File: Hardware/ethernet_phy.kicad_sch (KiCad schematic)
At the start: 17 parts, among them T1 WE-RJ45_7499010211A, U5 DP83822IRHBR

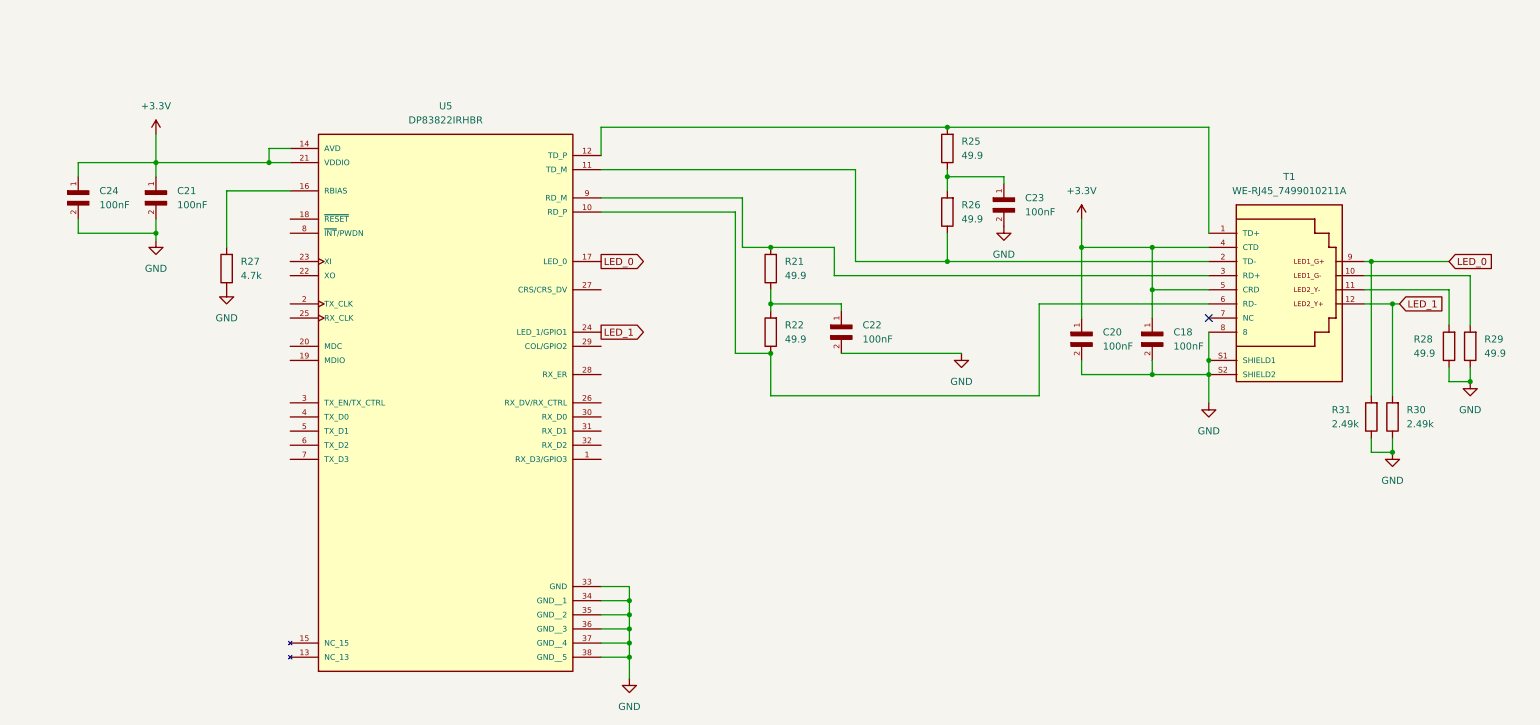
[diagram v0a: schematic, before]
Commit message: Finished Ethernet connection between MAC and PHY
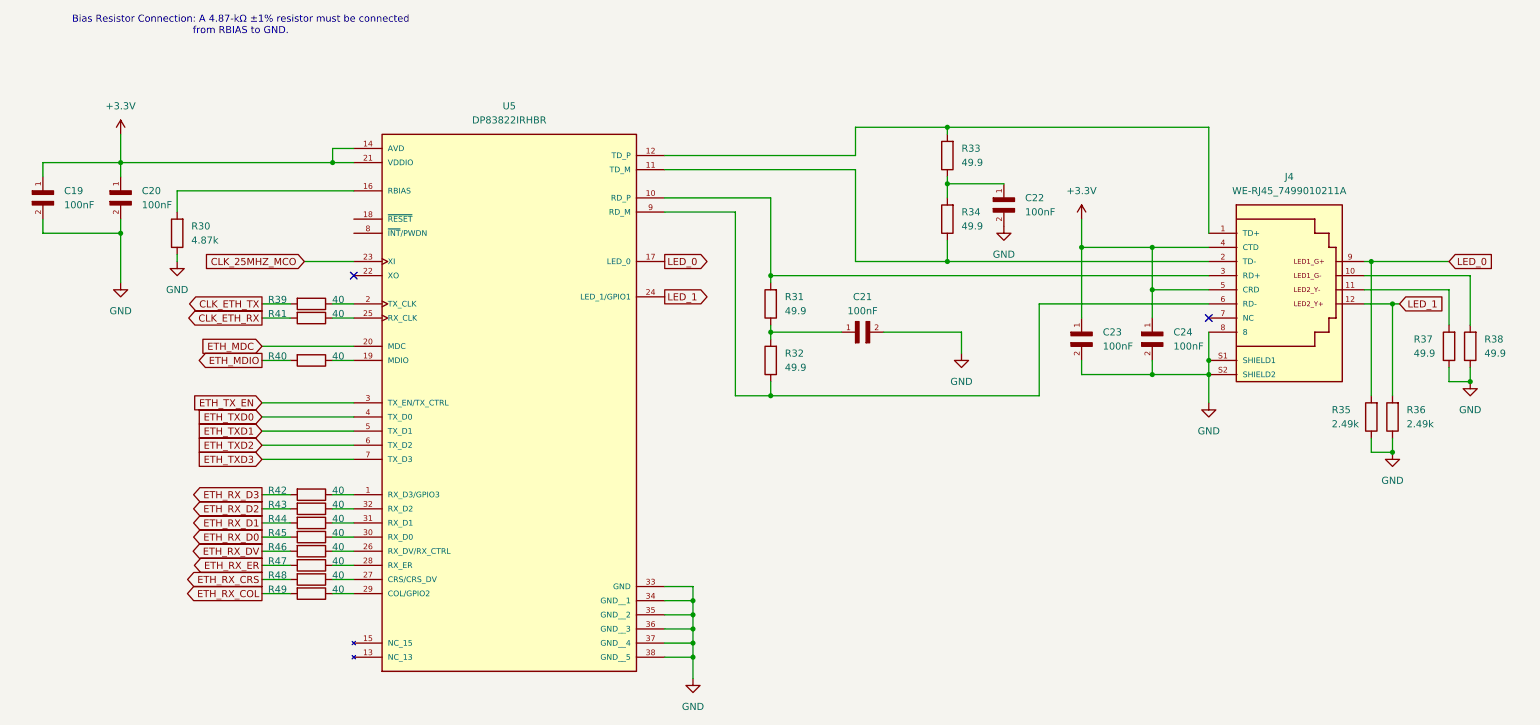
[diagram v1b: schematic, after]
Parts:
- added R39, R40, R41, R42, R43, R44, R45, R46, R47, R48, R49: 40, Resistor_SMD:R_0402_1005Metric, symbol Device:R
- R30: renamed from R27; value 4.7k -> 4.87k
- renumbered C24 to C19, C21 to C20, C22 to C21, C23 to C22, C20 to C23, C18 to C24, T1 to J4, R21 to R31, R22 to R32, R25 to R33, R26 to R34, R31 to R35, R30 to R36, R28 to R37, R29 to R38
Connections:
- net at U5.1 (RX_D3/GPIO3): now also R42.1
- net at J4.6 (RD-), R32.1: now also U5.9 (RD_M); no longer U5.10 (RD_P)
- net at U5.19 (MDIO): now also R40.1
- net at U5.2 (TX_CLK): now also R39.1
- net ETH_MDC: now reaches U5.20 (MDC)
- net CLK_25MHZ_MCO: now reaches U5.23 (XI)
- net at U5.25 (RX_CLK): now also R41.1
- net at U5.26 (RX_DV/RX_CTRL): now also R46.1
- net at U5.27 (CRS/CRS_DV): now also R48.1
- net at U5.28 (RX_ER): now also R47.1
- net at U5.29 (COL/GPIO2): now also R49.1
- net ETH_TX_EN: now reaches U5.3 (TX_EN/TX_CTRL)
- net at U5.30 (RX_D0): now also R45.1
- net at U5.31 (RX_D1): now also R44.1
- net at U5.32 (RX_D2): now also R43.1
- net ETH_TXD0: now reaches U5.4 (TX_D0)
- net ETH_TXD1: now reaches U5.5 (TX_D1)
- net ETH_TXD2: now reaches U5.6 (TX_D2)
- net ETH_TXD3: now reaches U5.7 (TX_D3)
- net at J4.3 (RD+), R31.2: now also U5.10 (RD_P); no longer U5.9 (RD_M)
- new net CLK_ETH_RX: R41.2
- new net CLK_ETH_TX: R39.2
- new net ETH_MDIO: R40.2
- new net ETH_RX_COL: R49.2
- new net ETH_RX_CRS: R48.2
- new net ETH_RX_D0: R45.2
- new net ETH_RX_D1: R44.2
- new net ETH_RX_D2: R43.2
- new net ETH_RX_D3: R42.2
- new net ETH_RX_DV: R46.2
- new net ETH_RX_ER: R47.2
- no-connect marks 1 -> 2
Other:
- note added: "Bias Resistor Connection: A 4.87-kΩ ±1% resistor must be connected from RBIAS to GND."
- moved on the sheet: C19, C20, C21, R30, R31, R32, R33, R34, U5

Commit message: Added high power USB-C Connection (5V @ 3A)
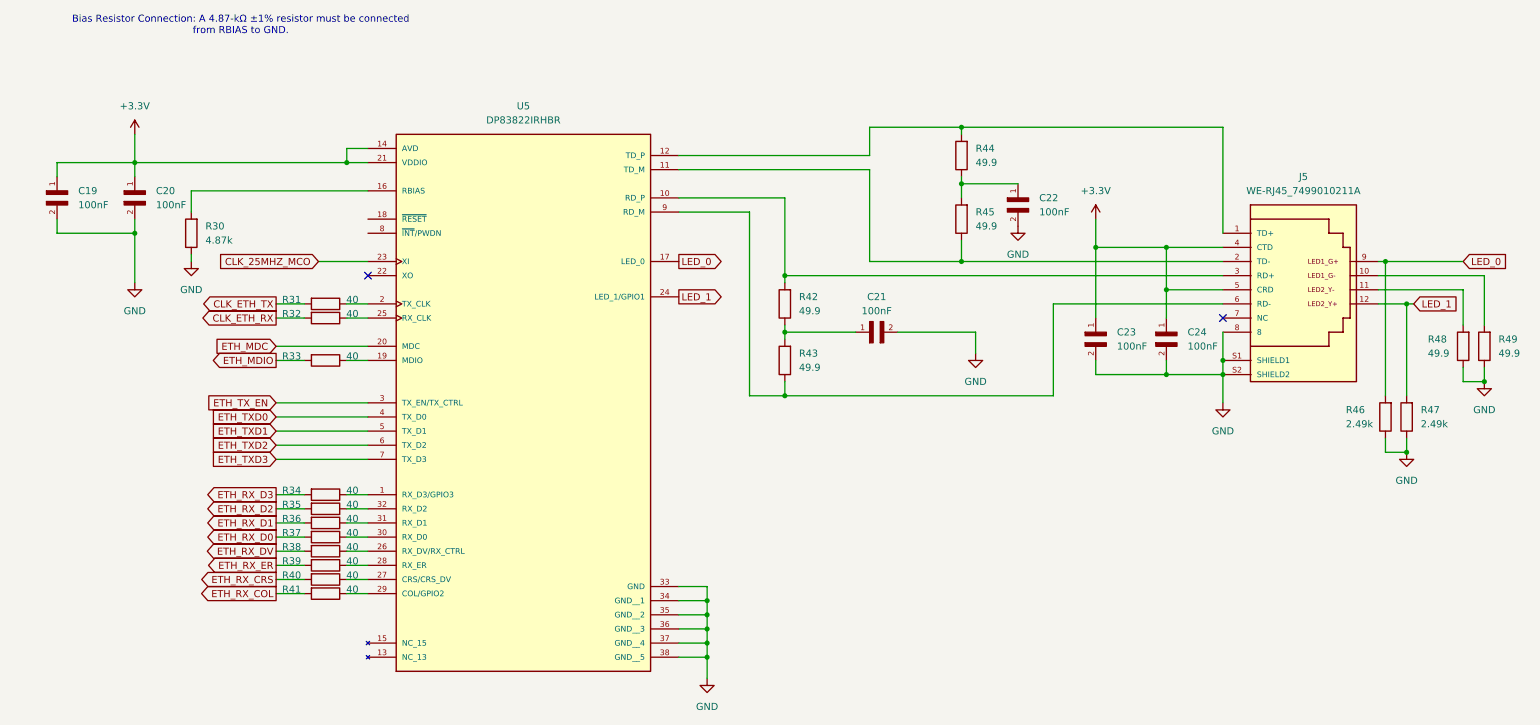
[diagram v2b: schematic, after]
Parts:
- renumbered J4 to J5, R39 to R31, R41 to R32, R40 to R33, R42 to R34, R43 to R35, R44 to R36, R45 to R37, R46 to R38, R47 to R39, R48 to R40, R49 to R41, R31 to R42, R32 to R43, R33 to R44, R34 to R45, R35 to R46, R36 to R47, R37 to R48, R38 to R49
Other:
- moved on the sheet: C19, C20, C21, C22, C23, C24, J5, R30, R31, R32, R33, R34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
